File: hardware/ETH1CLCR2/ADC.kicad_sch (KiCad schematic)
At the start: 86 parts, among them K501 TQ2SA-5V, Q501 BC847, U501 ADS8681IPWR, U502 AD8656, U503 OP1177AR, U504 AD8476_MSOP, U505 ADS8681IPWR, U506 CS5361, U507 AD8656, U508 OP1177AR, U509 AD8476_MSOP

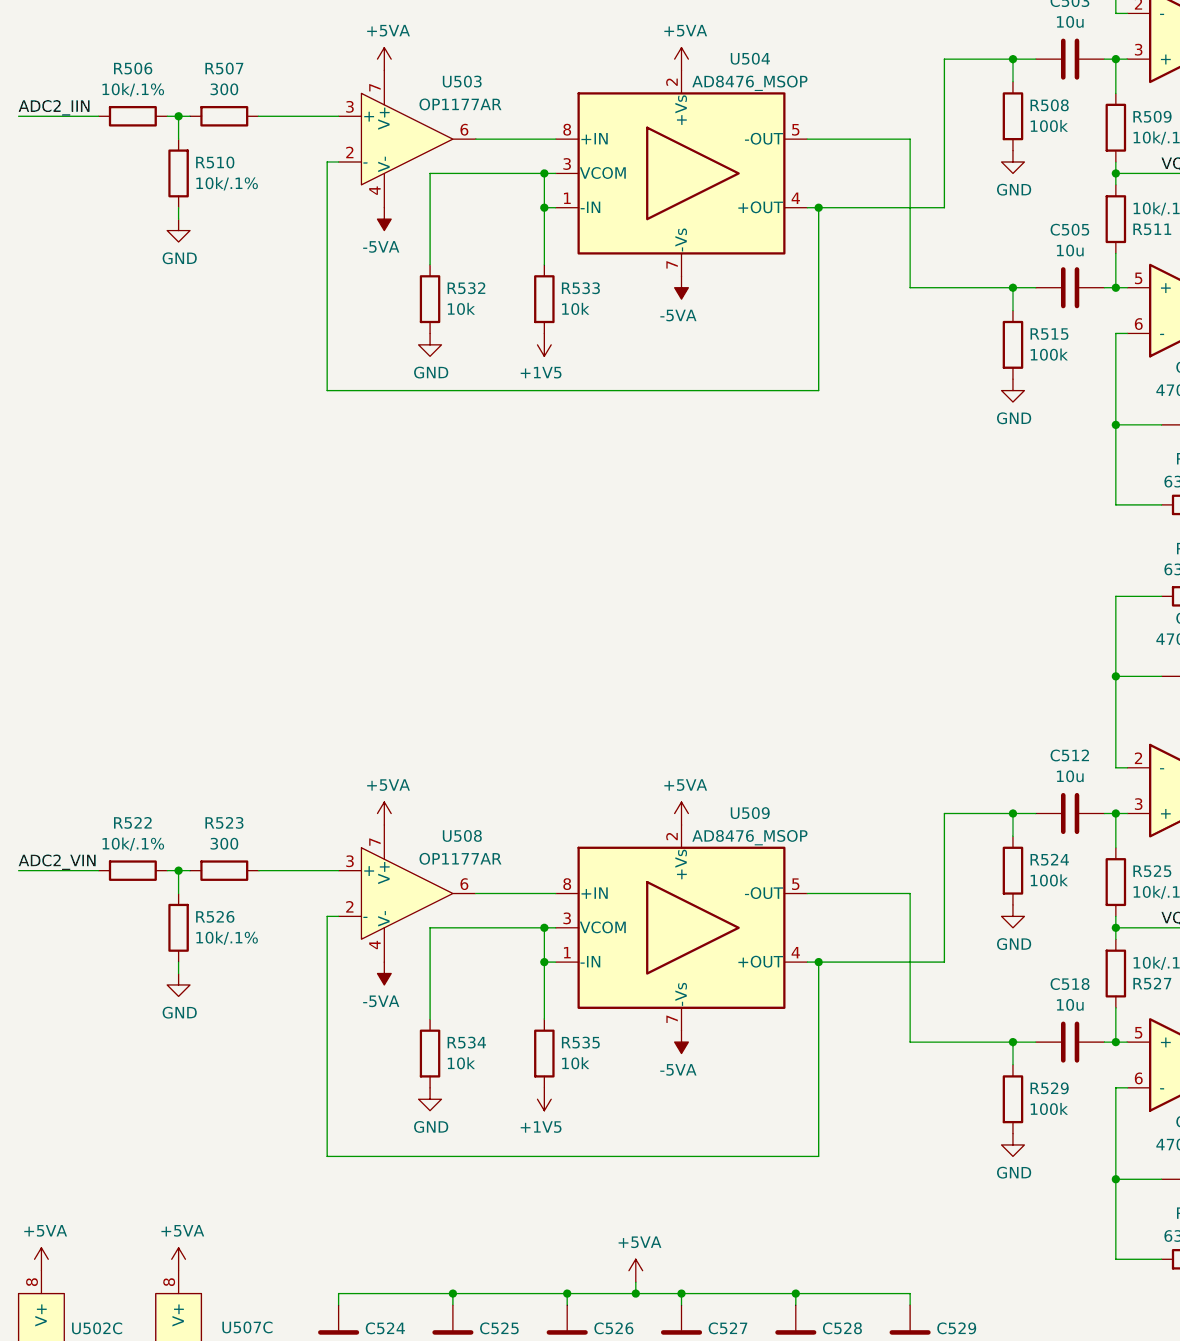
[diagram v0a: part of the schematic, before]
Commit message: Software development and added comments to the schematics.
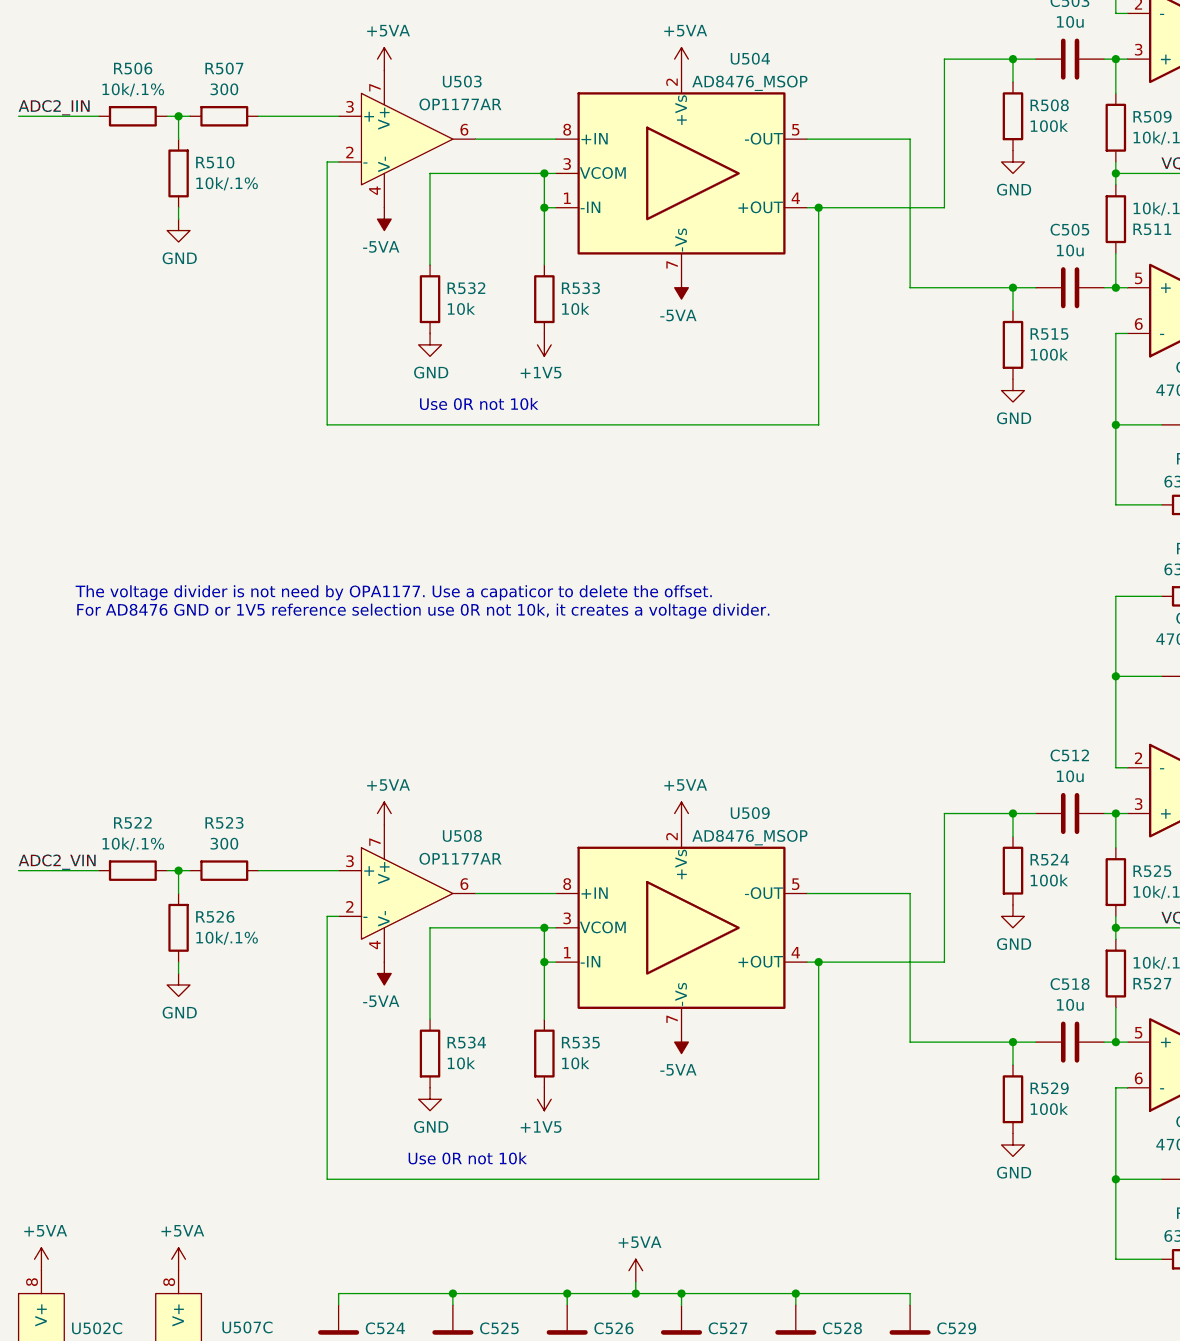
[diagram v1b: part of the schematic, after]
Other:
- note added: "The voltage divider is not need by OPA1177. Use a capaticor to delete the offset. For AD8476 GND or 1V5 reference selection use 0R not 10k, it creates a voltage divider."
- note added: "Use 0R not 10k"
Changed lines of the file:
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@@
     (stroke (width 0) (type default) (color 0 0 0 0))
   )
-  (wire (pts (xy 110.49 172.72) (xy 110.49 151.13))
+  (wire (pts (xy 110.49 175.26) (xy 110.49 151.13))
     (stroke (width 0) (type default) (color 0 0 0 0))
   )
@@
     (stroke (width 0) (type default) (color 0 0 0 0))
   )
-  (wire (pts (xy 55.88 87.63) (xy 110.49 87.63))
+  (wire (pts (xy 55.88 91.44) (xy 110.49 91.44))
     (stroke (width 0) (type default) (color 0 0 0 0))
   )
@@
     (stroke (width 0) (type default) (color 0 0 0 0))
   )
-  (wire (pts (xy 110.49 87.63) (xy 110.49 67.31))
+  (wire (pts (xy 110.49 91.44) (xy 110.49 67.31))
     (stroke (width 0) (type default) (color 0 0 0 0))
   )
@@
     (stroke (width 0) (type default) (color 0 0 0 0))
   )
-  (wire (pts (xy 55.88 146.05) (xy 55.88 172.72))
+  (wire (pts (xy 55.88 146.05) (xy 55.88 175.26))
     (stroke (width 0) (type default) (color 0 0 0 0))
   )
@@
     (stroke (width 0) (type default) (color 0 0 0 0))
   )
-  (wire (pts (xy 55.88 62.23) (xy 55.88 87.63))
+  (wire (pts (xy 55.88 62.23) (xy 55.88 91.44))
     (stroke (width 0) (type default) (color 0 0 0 0))
   )
@@
     (stroke (width 0) (type default) (color 0 0 0 0))
   )
-  (wire (pts (xy 55.88 172.72) (xy 110.49 172.72))
+  (wire (pts (xy 55.88 175.26) (xy 110.49 175.26))
     (stroke (width 0) (type default) (color 0 0 0 0))
   )
@@
     (stroke (width 0) (type default) (color 0 0 0 0))
   )
+  (text "The voltage divider is not need by OPA1177. Use a capaticor to delete the offset.\nFor AD8476 GND or 1V5 reference selection use 0R not 10k, it creates a voltage divider."
+    (at 27.94 113.03 0)
+    (effects (font (size 1.27 1.27)) (justify left bottom))
+  )
+  (text "Use 0R not 10k" (at 66.04 90.17 0)
+    (effects (font (size 1.27 1.27)) (justify left bottom))
+  )
+  (text "Use 0R not 10k" (at 64.77 173.99 0)
+    (effects (font (size 1.27 1.27)) (justify left bottom))
+  )
   (label "VQ" (at 151.13 147.32 180)

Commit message: Software development
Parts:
- R532, R533, R534, R535: value 10k -> (none)
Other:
- note added: "Connect pin 2 to GND for slave mode."
- note added: "Replace ADS8681 with AD7980."
- note added: "Replace R506 with 1u capacitor"
- note added: "Replace R522 with 1u capacitor"
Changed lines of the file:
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@@
+    (effects (font (size 1.27 1.27)) (justify left bottom))
+  )
+  (text "Replace ADS8681 with AD7980." (at 278.13 64.77 0)
     (effects (font (size 1.27 1.27)) (justify left bottom))
   )
@@
   )
   (text "Use 0R not 10k" (at 64.77 173.99 0)
+    (effects (font (size 1.27 1.27)) (justify left bottom))
+  )
+  (text "Replace R506 with 1u capacitor" (at 20.32 49.53 0)
+    (effects (font (size 1.27 1.27)) (justify left bottom))
+  )
+  (text "Replace R522 with 1u capacitor" (at 21.59 133.35 0)
+    (effects (font (size 1.27 1.27)) (justify left bottom))
+  )
+  (text "Connect pin 2 to GND for slave mode.\n" (at 195.58 149.86 0)
     (effects (font (size 1.27 1.27)) (justify left bottom))
   )
@@
       (effects (font (size 1.27 1.27)) (justify left))
     )
-    (property "Value" "10k" (id 1) (at 69.088 78.613 0)
+    (property "Value" "" (id 1) (at 69.088 78.613 0)
       (effects (font (size 1.27 1.27)) (justify left))
     )
@@
     (pin "2")
     (pin "3")
+    (pin "5")
+    (pin "6")
+    (pin "7")
+    (pin "4")
+    (pin "8")
   )
   (symbol (lib_id "ETH1CLCR2:AD8656") (at 151.13 78.74 0) (mirror x) (unit 2)
@@
       (effects (font (size 1.27 1.27)) hide)
     )
+    (pin "1")
+    (pin "2")
+    (pin "3")
     (pin "5")
     (pin "6")
     (pin "7")
+    (pin "4")
+    (pin "8")
   )
   (symbol (lib_id "ETH1CLCR2:AD8656") (at 24.13 193.04 0) (unit 3)
@@
       (effects (font (size 1.27 1.27)) hide)
     )
+    (pin "1")
+    (pin "2")
+    (pin "3")
+    (pin "5")
+    (pin "6")
+    (pin "7")
     (pin "4")
     (pin "8")
@@
       (effects (font (size 1.27 1.27)) (justify left))
     )
-    (property "Value" "10k" (id 1) (at 81.788 78.613 0)
+    (property "Value" "" (id 1) (at 81.788 78.613 0)
       (effects (font (size 1.27 1.27)) (justify left))
     )
@@
       (effects (font (size 1.27 1.27)) (justify left))
     )
-    (property "Value" "10k" (id 1) (at 69.088 162.433 0)
+    (property "Value" "" (id 1) (at 69.088 162.433 0)
       (effects (font (size 1.27 1.27)) (justify left))
     )
@@
       (effects (font (size 1.27 1.27)) (justify left))
     )
-    (property "Value" "10k" (id 1) (at 81.788 162.433 0)
+    (property "Value" "" (id 1) (at 81.788 162.433 0)
       (effects (font (size 1.27 1.27)) (justify left))
     )
@@
     (pin "2")
     (pin "3")
+    (pin "5")
+    (pin "6")
+    (pin "7")
+    (pin "4")
+    (pin "8")
   )
   (symbol (lib_id "Device:C") (at 152.4 119.38 270) (unit 1)
@@
       (effects (font (size 1.27 1.27)) hide)
     )
+    (pin "1")
+    (pin "2")
+    (pin "3")
     (pin "5")
     (pin "6")
     (pin "7")
+    (pin "4")
+    (pin "8")
   )
   (symbol (lib_id "Device:C") (at 172.72 147.32 0) (unit 1)
@@
       (effects (font (size 1.27 1.27)) hide)
     )
+    (pin "1")
+    (pin "2")
+    (pin "3")
+    (pin "5")
+    (pin "6")
+    (pin "7")
     (pin "4")
     (pin "8")

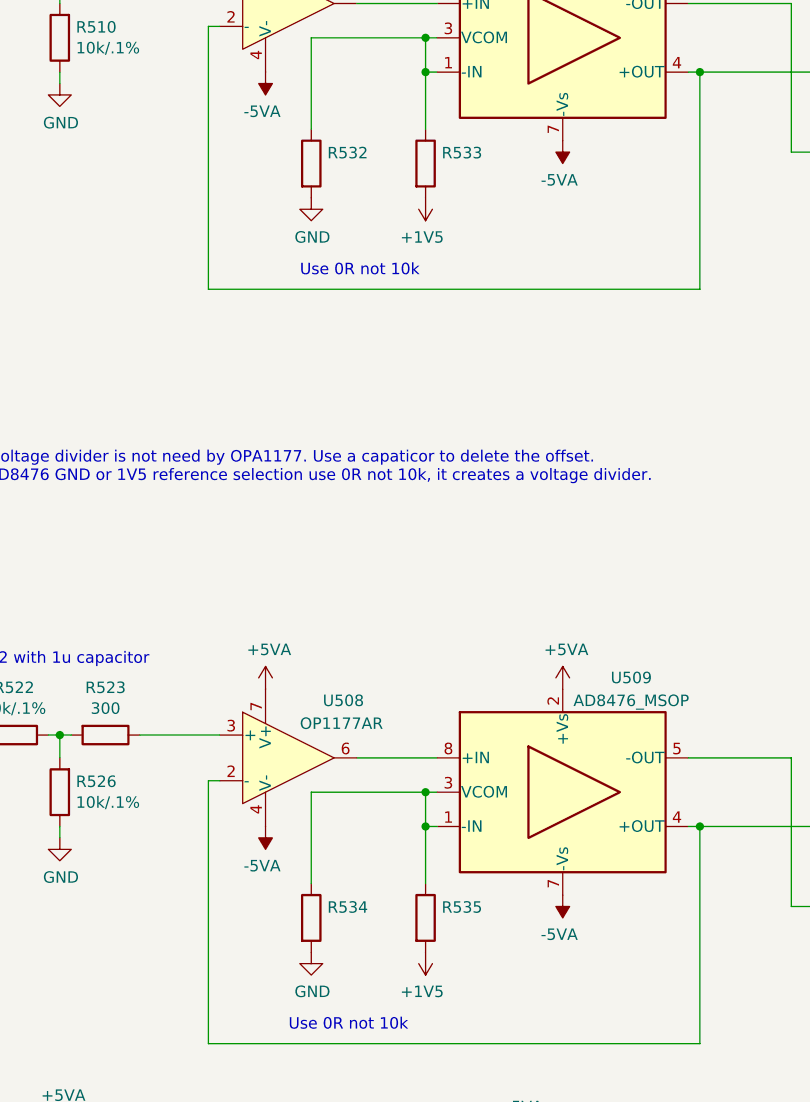
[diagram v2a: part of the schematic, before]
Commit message: Converted HW files to KiCAD 7.0.
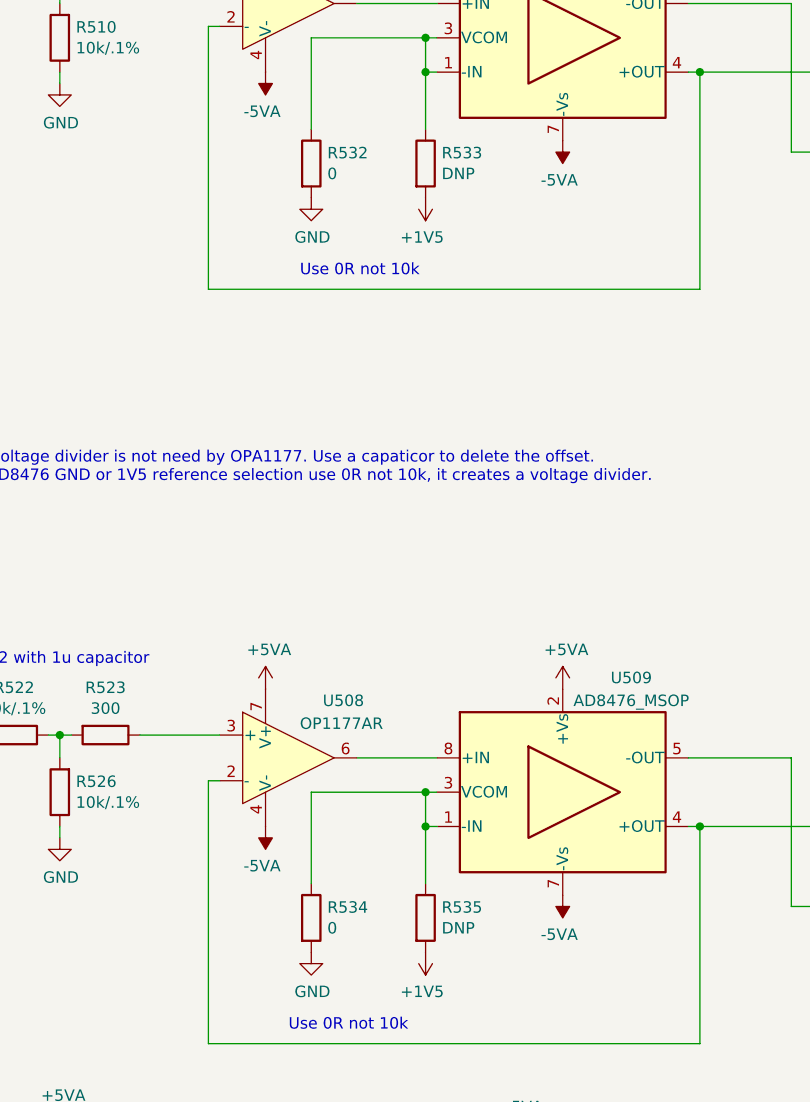
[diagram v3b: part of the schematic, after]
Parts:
- R532, R534: value (none) -> 0
- R533, R535: value (none) -> DNP
